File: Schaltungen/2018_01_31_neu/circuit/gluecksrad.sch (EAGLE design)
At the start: 17 parts, among them IC1 LOGIK_SHIFT8, IC2 ULN2003AD

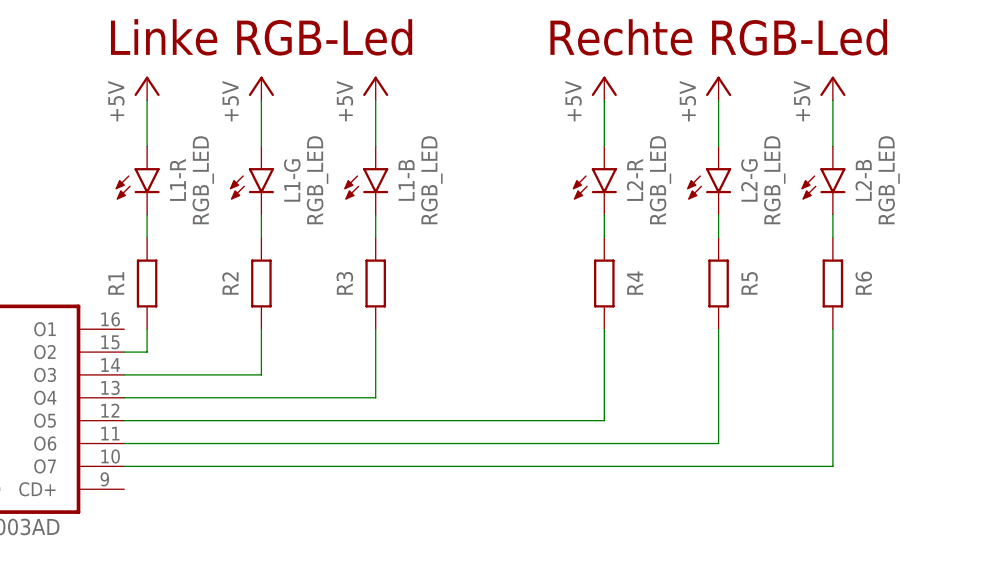
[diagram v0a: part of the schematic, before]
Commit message: updated LED-Platine (added values for resistors)
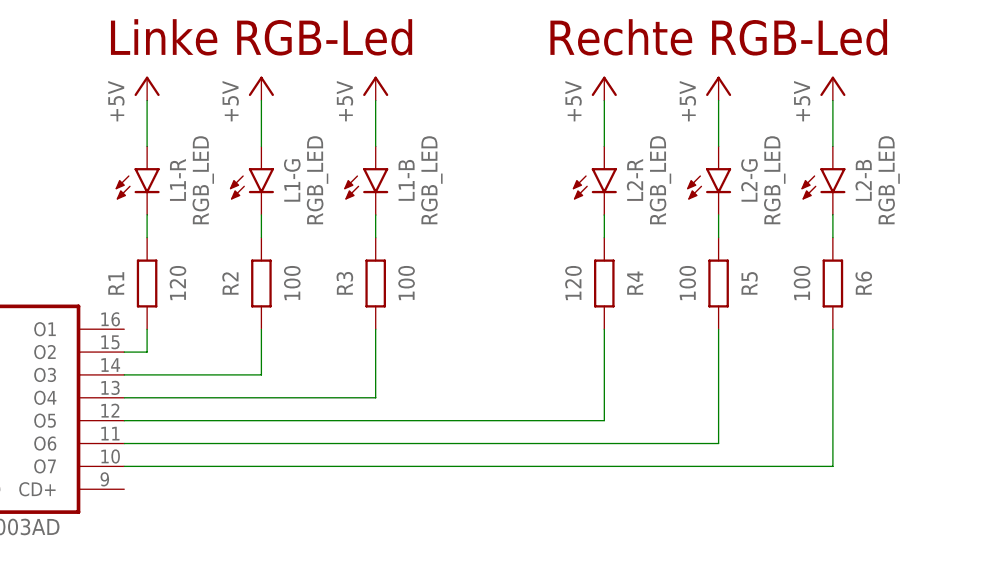
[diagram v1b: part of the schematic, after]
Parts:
- R1, R4: value (none) -> 120
- R2, R3, R5, R6: value (none) -> 100
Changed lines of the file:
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@@
 <part name="P+3" library="supply1" deviceset="+5V" device=""/>
 <part name="P+4" library="supply1" deviceset="+5V" device=""/>
-<part name="R1" library="robo_ag" deviceset="RESISTOR" device="-10MM"/>
-<part name="R2" library="robo_ag" deviceset="RESISTOR" device="-10MM"/>
-<part name="R3" library="robo_ag" deviceset="RESISTOR" device="-10MM"/>
+<part name="R1" library="robo_ag" deviceset="RESISTOR" device="-10MM" value="120"/>
+<part name="R2" library="robo_ag" deviceset="RESISTOR" device="-10MM" value="100"/>
+<part name="R3" library="robo_ag" deviceset="RESISTOR" device="-10MM" value="100"/>
 <part name="P+5" library="supply1" deviceset="+5V" device=""/>
-<part name="R4" library="robo_ag" deviceset="RESISTOR" device="-10MM"/>
-<part name="R5" library="robo_ag" deviceset="RESISTOR" device="-10MM"/>
-<part name="R6" library="robo_ag" deviceset="RESISTOR" device="-10MM"/>
+<part name="R4" library="robo_ag" deviceset="RESISTOR" device="-10MM" value="120"/>
+<part name="R5" library="robo_ag" deviceset="RESISTOR" device="-10MM" value="100"/>
+<part name="R6" library="robo_ag" deviceset="RESISTOR" device="-10MM" value="100"/>
 <part name="P+6" library="supply1" deviceset="+5V" device=""/>
 <part name="P+7" library="supply1" deviceset="+5V" device=""/>
